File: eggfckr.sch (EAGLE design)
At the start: 7 parts, among them IC1 LM555N

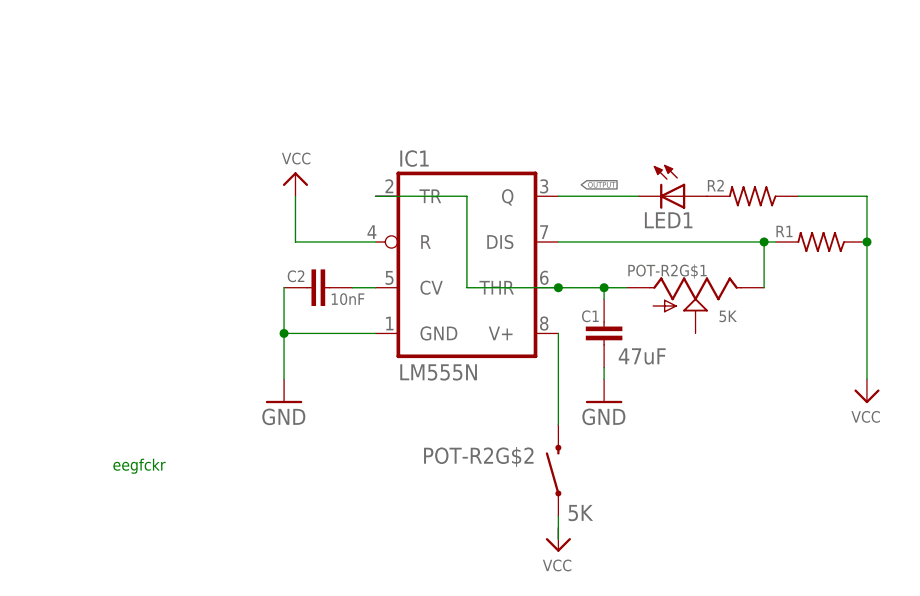
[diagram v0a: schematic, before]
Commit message: attiny85 version
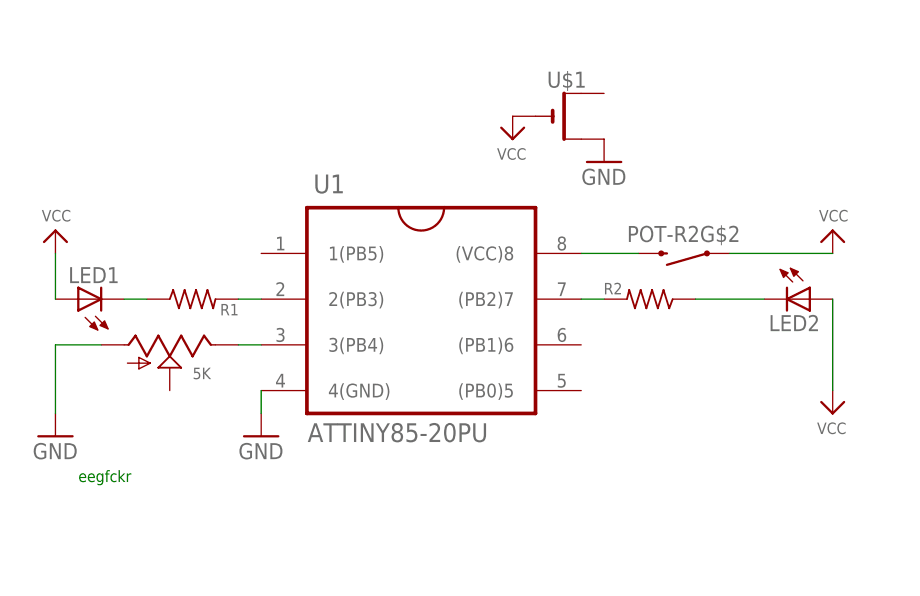
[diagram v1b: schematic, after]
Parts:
- removed C1: 47uF, ATtami:CAP0805
- removed C2: 10nF, ATtami:CAP0805
- removed IC1: LM555N, adafruit:LM555N
- added LED2: (no value), adafruit:LED3MM
- added U$1: (no value), adafruit:CR2032THM
- added U1: ATTINY85-20PU, Atmel_By_element14_Batch_1-00:ATTINY85-20PU
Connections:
- removed net N$5: IC1.V+, POT-R2G$2.2
- removed net OUTPUT: IC1.Q, LED1.C
- new net N$7: LED2.C, R2.1
- net GND: now also POT-R2G$1.A, U$1.+1, U1.4(GND); no longer C1.2, C2.1, IC1.GND
- net N$1: now also R2.2, U1.(PB2)7; no longer C2.2, IC1.CV
- net N$2: now also POT-R2G$1.E, U1.3(PB4); no longer C1.1, IC1.THR, IC1.TR, POT-R2G$1.A
- net N$3: now also POT-R2G$2.2, U1.(VCC)8; no longer POT-R2G$2.1
- net N$4: now also U1.2(PB3); no longer IC1.DIS, POT-R2G$1.E
- net N$6: now also LED1.C, R1.1; no longer LED1.A, R2.2
- net VCC: now also LED1.A, LED2.A, POT-R2G$2.1, U$1.-; no longer IC1.R, R1.1, R2.1
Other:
- moved on the sheet: LED1, POT-R2G$2, R1, R2

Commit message: failed linear to log pot convertion
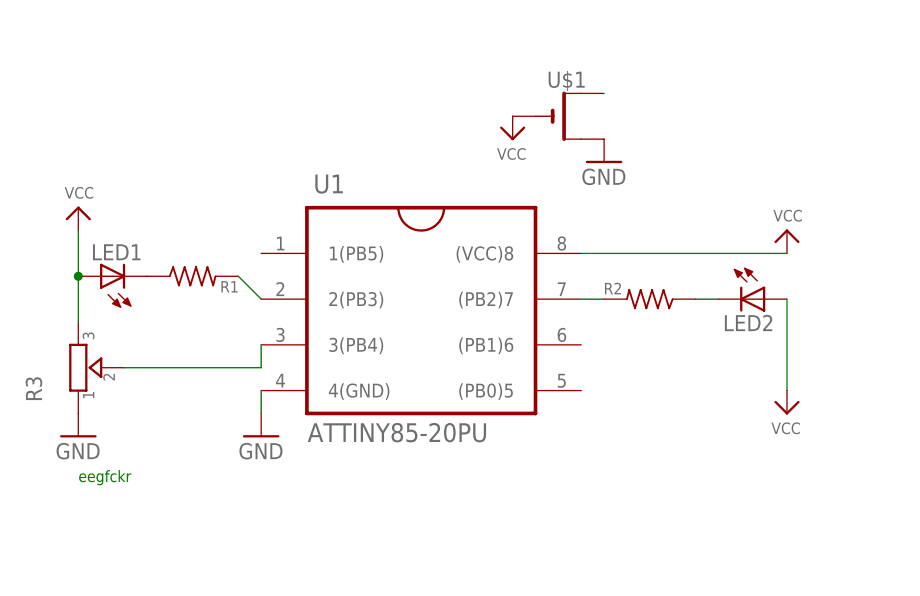
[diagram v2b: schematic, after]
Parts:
- removed POT-R2: 5K, SparkFun-Electromechanical:POT_SWITCHPOT_PTH
- added R3: (no value), dp_devices:TRIMMER-3306F
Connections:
- removed net N$3: POT-R2G$2.2, U1.(VCC)8
- net GND: now also R3.1; no longer POT-R2G$1.A
- net N$2: now also R3.2; no longer POT-R2G$1.E
- net VCC: now also R3.3, U1.(VCC)8; no longer POT-R2G$2.1
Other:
- moved on the sheet: LED1, LED2, R1
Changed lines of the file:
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@@
 <setting verticaltext="up"/>
 </settings>
-<grid distance="100" unitdist="mil" unit="mil" style="lines" multiple="1" display="no" altdistance="50" altunitdist="mil" altunit="mil"/>
+<grid distance="0.1" unitdist="inch" unit="inch" style="lines" multiple="1" display="no" altdistance="0.01" altunitdist="inch" altunit="inch"/>
 <layers>
 <layer number="1" name="Top" color="4" fill="1" visible="no" active="no"/>
@@
 <parts>
 <part name="P+1" library="ATTiny Fuse Reset with 12V Charge Pump" deviceset="VCC" device=""/>
-<part name="POT-R2" library="SparkFun-Electromechanical" deviceset="POT_SWITCH" device="POT_PTH" value="5K"/>
 <part name="LED1" library="adafruit" deviceset="LED" device="3MM"/>
 <part name="R2" library="adafruit" deviceset="R-US_" device="0204/7"/>
@@
 <part name="P+4" library="ATTiny Fuse Reset with 12V Charge Pump" deviceset="VCC" device=""/>
 <part name="GND3" library="ATtami" deviceset="GND" device=""/>
+<part name="R3" library="dp_devices" deviceset="TRIMMER" device="-3306F"/>
 </parts>
 <sheets>
@@
 </plain>
 <instances>
-<instance part="P+1" gate="VCC" x="83.82" y="27.94"/>
-<instance part="POT-R2" gate="G$1" x="10.16" y="15.24" smashed="yes" rot="R270">
-<attribute name="VALUE" x="12.7" y="11.43" size="1.27" layer="95"/>
-</instance>
-<instance part="POT-R2" gate="G$2" x="67.31" y="25.4" smashed="yes" rot="R180">
-<attribute name="NAME" x="60.96" y="26.67" size="1.778" layer="95"/>
-</instance>
-<instance part="LED1" gate="G$1" x="0" y="20.32" rot="R90"/>
+<instance part="P+1" gate="VCC" x="78.74" y="27.94"/>
+<instance part="LED1" gate="G$1" x="2.54" y="22.86" rot="R90"/>
 <instance part="R2" gate="G$1" x="63.5" y="20.32" smashed="yes" rot="R180">
 <attribute name="NAME" x="60.452" y="22.1234" size="1.27" layer="95" rot="R180"/>
@@
 <attribute name="VALUE" x="25.4762" y="4.445" size="2.0828" layer="96" ratio="10" rot="SR0"/>
 </instance>
-<instance part="R1" gate="G$1" x="12.7" y="20.32" smashed="yes">
-<attribute name="NAME" x="15.748" y="18.5166" size="1.27" layer="95"/>
-<attribute name="VALUE" x="8.89" y="17.018" size="1.778" layer="96"/>
+<instance part="R1" gate="G$1" x="12.7" y="22.86" smashed="yes">
+<attribute name="NAME" x="15.748" y="21.0566" size="1.27" layer="95"/>
+<attribute name="VALUE" x="8.89" y="19.558" size="1.778" layer="96"/>
 </instance>
-<instance part="LED2" gate="G$1" x="81.28" y="20.32" rot="R270"/>
-<instance part="GND2" gate="1" x="-2.54" y="5.08"/>
-<instance part="P+2" gate="VCC" x="83.82" y="7.62" rot="R180"/>
+<instance part="LED2" gate="G$1" x="76.2" y="20.32" rot="R270"/>
+<instance part="GND2" gate="1" x="0" y="5.08"/>
+<instance part="P+2" gate="VCC" x="78.74" y="7.62" rot="R180"/>
 <instance part="GND1" gate="1" x="20.32" y="5.08"/>
-<instance part="P+3" gate="VCC" x="-2.54" y="27.94"/>
+<instance part="P+3" gate="VCC" x="0" y="30.48"/>
 <instance part="U$1" gate="G$1" x="53.34" y="40.64"/>
 <instance part="P+4" gate="VCC" x="48.26" y="38.1" rot="R180"/>
 <instance part="GND3" gate="1" x="58.42" y="35.56"/>
+<instance part="R3" gate="R" x="0" y="12.7" rot="R90"/>
 </instances>
 <busses>
@@
 <pinref part="R1" gate="G$1" pin="1"/>
 <pinref part="LED1" gate="G$1" pin="C"/>
-<wire x1="5.08" y1="20.32" x2="7.62" y2="20.32" width="0.1524" layer="91"/>
 </segment>
 </net>
@@
 <pinref part="R2" gate="G$1" pin="1"/>
 <pinref part="LED2" gate="G$1" pin="C"/>
-<wire x1="76.2" y1="20.32" x2="68.58" y2="20.32" width="0.1524" layer="91"/>
+<wire x1="71.12" y1="20.32" x2="68.58" y2="20.32" width="0.1524" layer="91"/>
 </segment>
 </net>
@@
 </segment>
 <segment>
-<pinref part="POT-R2" gate="G$1" pin="A"/>
-<pinref part="GND2" gate="1" pin="GND"/>
-<wire x1="2.54" y1="15.24" x2="-2.54" y2="15.24" width="0.1524" layer="91"/>
-<wire x1="-2.54" y1="15.24" x2="-2.54" y2="7.62" width="0.1524" layer="91"/>
-</segment>
-<segment>
 <pinref part="U$1" gate="G$1" pin="+1"/>
 <pinref part="GND3" gate="1" pin="GND"/>
 </segment>
+<segment>
+<pinref part="R3" gate="R" pin="1"/>
+<pinref part="GND2" gate="1" pin="GND"/>
+</segment>
 </net>
 <net name="VCC" class="0">
 <segment>
-<pinref part="POT-R2" gate="G$2" pin="1"/>
-<wire x1="72.39" y1="25.4" x2="83.82" y2="25.4" width="0.1524" layer="91"/>
 <pinref part="P+1" gate="VCC" pin="VCC"/>
+<pinref part="U1" gate="A" pin="(VCC)8"/>
+<wire x1="55.88" y1="25.4" x2="78.74" y2="25.4" width="0.1524" layer="91"/>
 </segment>
 <segment>
 <pinref part="LED2" gate="G$1" pin="A"/>
 <pinref part="P+2" gate="VCC" pin="VCC"/>
-<wire x1="83.82" y1="20.32" x2="83.82" y2="10.16" width="0.1524" layer="91"/>
+<wire x1="78.74" y1="20.32" x2="78.74" y2="10.16" width="0.1524" layer="91"/>
 </segment>
 <segment>
 <pinref part="LED1" gate="G$1" pin="A"/>
 <pinref part="P+3" gate="VCC" pin="VCC"/>
-<wire x1="-2.54" y1="20.32" x2="-2.54" y2="25.4" width="0.1524" layer="91"/>
+<wire x1="0" y1="22.86" x2="0" y2="27.94" width="0.1524" layer="91"/>
+<wire x1="0" y1="22.86" x2="0" y2="17.78" width="0.1524" layer="91"/>
+<junction x="0" y="22.86"/>
+<pinref part="R3" gate="R" pin="3"/>
 </segment>
 <segment>
@@
 </segment>
 </net>
-<net name="N$3" class="0">
-<segment>
-<pinref part="U1" gate="A" pin="(VCC)8"/>
-<wire x1="55.88" y1="25.4" x2="62.23" y2="25.4" width="0.1524" layer="91"/>
-<pinref part="POT-R2" gate="G$2" pin="2"/>
-</segment>
-</net>
-<net name="N$2" class="0">
-<segment>
-<pinref part="U1" gate="A" pin="3(PB4)"/>
-<pinref part="POT-R2" gate="G$1" pin="E"/>
-<wire x1="20.32" y1="15.24" x2="17.78" y2="15.24" width="0.1524" layer="91"/>
-</segment>
-</net>
 <net name="N$4" class="0">
 <segment>
 <pinref part="U1" gate="A" pin="2(PB3)"/>
 <pinref part="R1" gate="G$1" pin="2"/>
-<wire x1="20.32" y1="20.32" x2="17.78" y2="20.32" width="0.1524" layer="91"/>
-</segment>
-</net>
+<wire x1="20.32" y1="20.32" x2="17.78" y2="22.86" width="0.1524" layer="91"/>
+</segment>
+</net>
+<net name="N$2" class="0">
+<segment>
+<pinref part="U1" gate="A" pin="3(PB4)"/>
+<wire x1="20.32" y1="12.7" x2="20.32" y2="15.24" width="0.1524" layer="91"/>
+<pinref part="R3" gate="R" pin="2"/>
+<wire x1="5.08" y1="12.7" x2="20.32" y2="12.7" width="0.1524" layer="91"/>
+</segment>
+</net>

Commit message: silluate circuit
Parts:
- removed U$1: (no value), adafruit:CR2032THM
- added GND, VCC: (no value), microbuilder:HEADER-1X1ROUND
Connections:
- net GND: now also GND.1; no longer U$1.+1
- net VCC: now also VCC.1; no longer U$1.-
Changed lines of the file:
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@@
 <part name="GND1" library="ATtami" deviceset="GND" device=""/>
 <part name="P+3" library="ATTiny Fuse Reset with 12V Charge Pump" deviceset="VCC" device=""/>
-<part name="U$1" library="adafruit" deviceset="CR2032" device="THM"/>
 <part name="P+4" library="ATTiny Fuse Reset with 12V Charge Pump" deviceset="VCC" device=""/>
 <part name="GND3" library="ATtami" deviceset="GND" device=""/>
 <part name="R3" library="dp_devices" deviceset="TRIMMER" device="-3306F"/>
+<part name="GND" library="microbuilder" deviceset="HEADER-1X1" device="ROUND"/>
+<part name="VCC" library="microbuilder" deviceset="HEADER-1X1" device="ROUND"/>
 </parts>
 <sheets>
@@
 <instance part="GND1" gate="1" x="20.32" y="5.08"/>
 <instance part="P+3" gate="VCC" x="0" y="30.48"/>
-<instance part="U$1" gate="G$1" x="53.34" y="40.64"/>
 <instance part="P+4" gate="VCC" x="48.26" y="38.1" rot="R180"/>
-<instance part="GND3" gate="1" x="58.42" y="35.56"/>
+<instance part="GND3" gate="1" x="58.42" y="38.1"/>
 <instance part="R3" gate="R" x="0" y="12.7" rot="R90"/>
+<instance part="GND" gate="G$1" x="60.96" y="45.72" smashed="yes">
+<attribute name="NAME" x="54.61" y="48.895" size="1.778" layer="95"/>
+<attribute name="VALUE" x="54.61" y="40.64" size="1.778" layer="96"/>
+</instance>
+<instance part="VCC" gate="G$1" x="50.8" y="45.72" smashed="yes">
+<attribute name="NAME" x="44.45" y="48.895" size="1.778" layer="95"/>
+<attribute name="VALUE" x="44.45" y="40.64" size="1.778" layer="96"/>
+</instance>
 </instances>
 <busses>
@@
 </segment>
 <segment>
-<pinref part="U$1" gate="G$1" pin="+1"/>
-<pinref part="GND3" gate="1" pin="GND"/>
+<pinref part="R3" gate="R" pin="1"/>
+<pinref part="GND2" gate="1" pin="GND"/>
 </segment>
 <segment>
-<pinref part="R3" gate="R" pin="1"/>
-<pinref part="GND2" gate="1" pin="GND"/>
+<pinref part="GND3" gate="1" pin="GND"/>
+<pinref part="GND" gate="G$1" pin="1"/>
+<wire x1="58.42" y1="45.72" x2="58.42" y2="40.64" width="0.1524" layer="91"/>
 </segment>
 </net>
@@
 </segment>
 <segment>
-<pinref part="U$1" gate="G$1" pin="-"/>
 <pinref part="P+4" gate="VCC" pin="VCC"/>
+<pinref part="VCC" gate="G$1" pin="1"/>
+<wire x1="48.26" y1="45.72" x2="48.26" y2="40.64" width="0.1524" layer="91"/>
 </segment>
 </net>

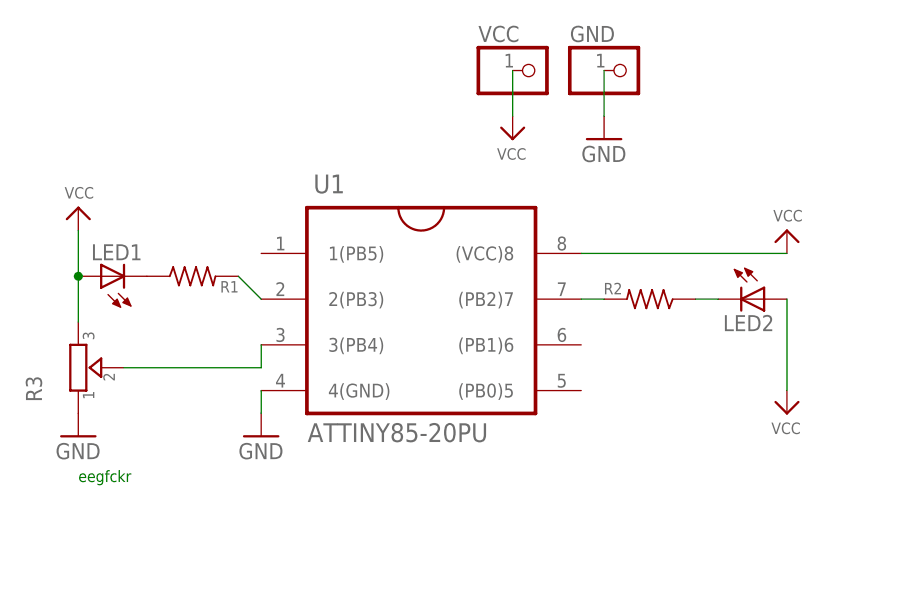
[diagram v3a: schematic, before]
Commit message: add lib with costum audio jack
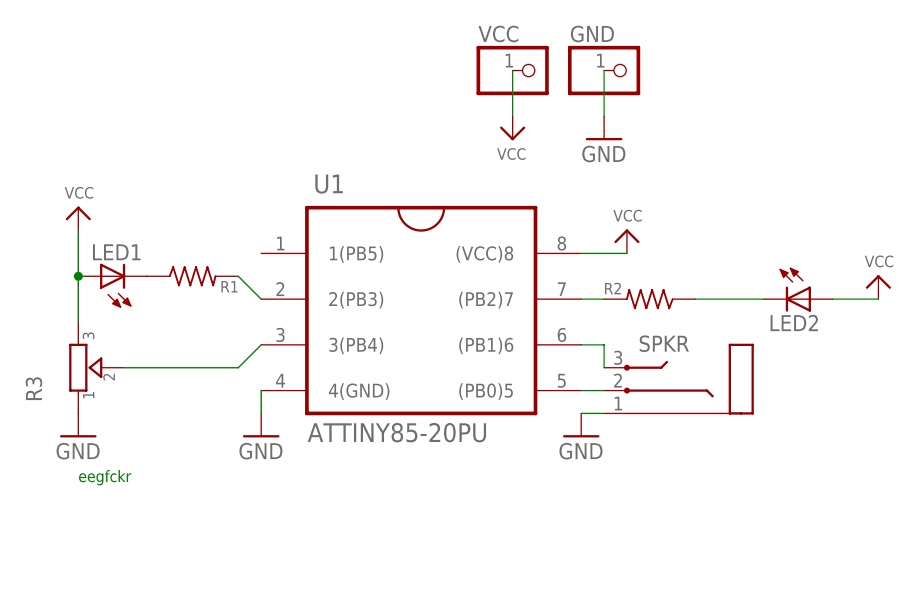
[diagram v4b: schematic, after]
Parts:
- added SPKR: (no value), eggfckr:AUDIO_STEREOJACK
- GND, VCC: device microbuilder:HEADER-1X1ROUND -> eggfckr:HEADER-1X1
- R1, R2: device adafruit:R-US_0204/7 -> eggfckr:R-US_0207/7
- R3: device dp_devices:TRIMMER-3306F -> eggfckr:TRIMMER-3306F
- U1: device Atmel_By_element14_Batch_1-00:ATTINY85-20PU -> eggfckr:ATTINY85-20PU
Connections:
- new net N$3: SPKR.3, U1.(PB1)6
- new net N$5: SPKR.2, U1.(PB0)5
- net GND: now also SPKR.1
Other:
- moved on the sheet: LED2
